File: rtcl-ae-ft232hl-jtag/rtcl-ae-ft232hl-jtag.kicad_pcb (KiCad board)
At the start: 2 copper layers, 20.3 x 52.1 mm, 3 parts, among them J1 Conn_01x14, J2 Conn_01x14, J3 Conn_01x06

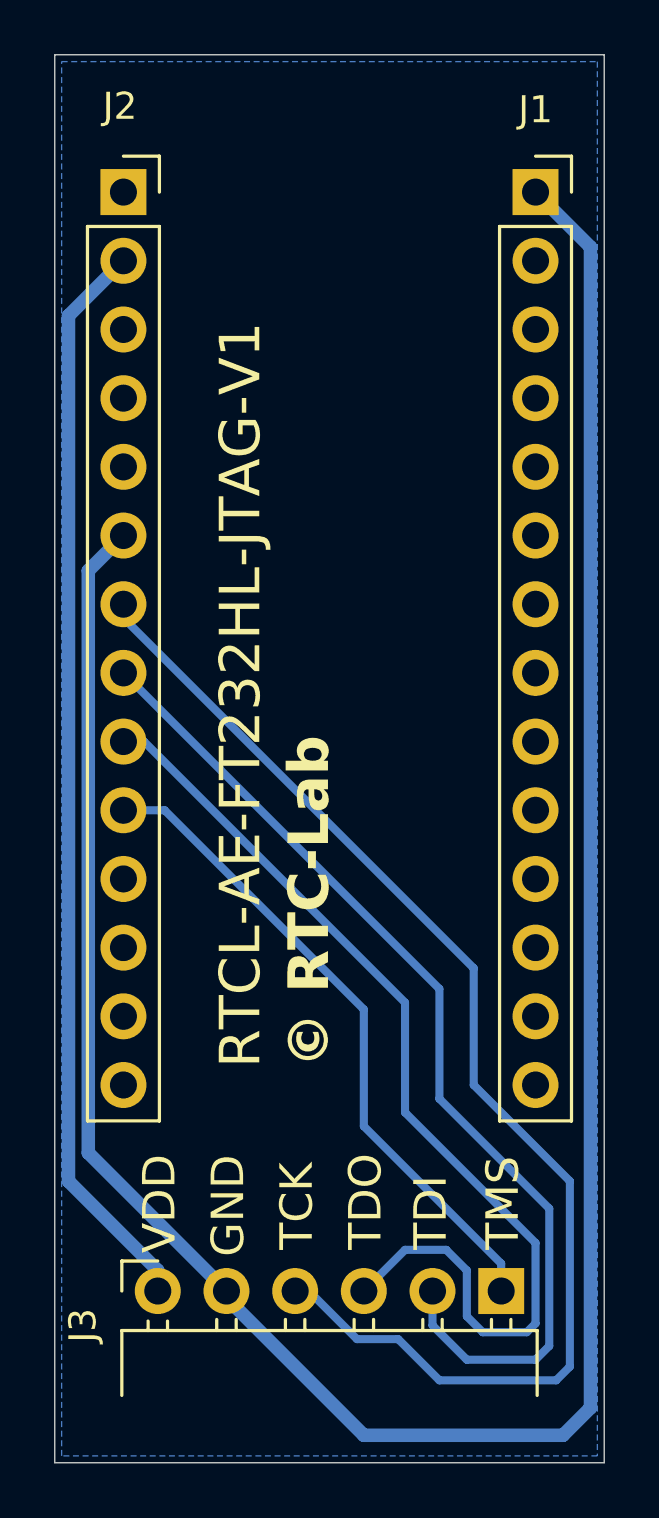
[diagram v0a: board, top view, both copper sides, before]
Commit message: Update KiCad project settings for improved layer visibility and clearance
- Changed active layer from 2 to 7 in the .kicad_prl file to enhance design focus.
- Updated layer visibility settings: enabled text display and disabled track display.
- Adjusted zone display mode from 0 to 1 for better zone management.
- Modified solder mask to copper clearance from 0.0 to 0.005 in the .kicad_pro file for improved manufacturing tolerances.
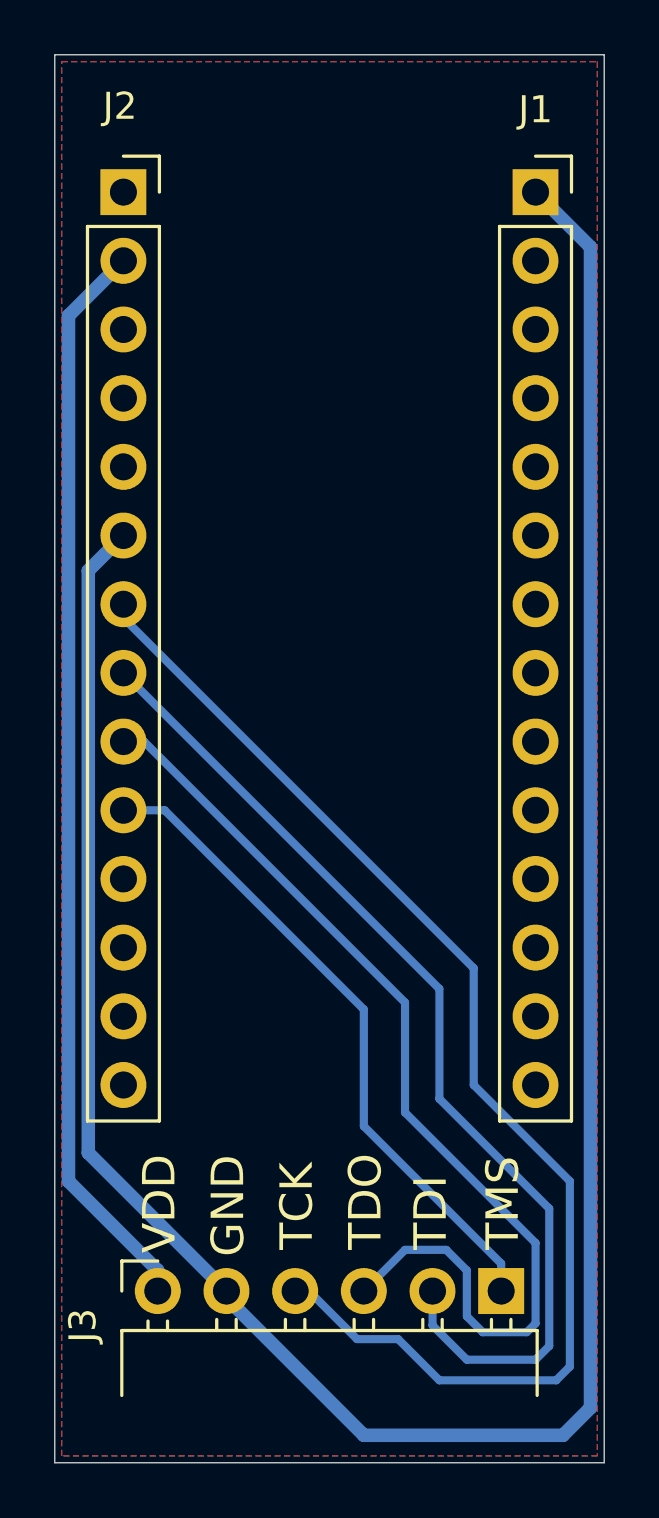
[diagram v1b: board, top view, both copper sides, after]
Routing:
- added copper zone on F.Cu, net GND
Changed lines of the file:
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@@
+		)
+	)
+	(gr_text "VDD"
+		(at 119.888 125.476 -90)
+		(layer "B.SilkS")
+		(effects
+			(font
+				(size 1.2 1.2)
+				(thickness 0.15)
+			)
+			(justify left bottom mirror)
+		)
+	)
+	(gr_text "GND"
+		(at 122.428 125.73 -90)
+		(layer "B.SilkS")
+		(effects
+			(font
+				(size 1.2 1.2)
+				(thickness 0.15)
+			)
+			(justify left bottom mirror)
+		)
+	)
+	(gr_text "TCK"
+		(at 124.968 125.476 -90)
+		(layer "B.SilkS")
+		(effects
+			(font
+				(size 1.2 1.2)
+				(thickness 0.15)
+			)
+			(justify left bottom mirror)
+		)
+	)
+	(gr_text "TDO"
+		(at 127.508 125.476 -90)
+		(layer "B.SilkS")
+		(effects
+			(font
+				(size 1.2 1.2)
+				(thickness 0.15)
+			)
+			(justify left bottom mirror)
+		)
+	)
+	(gr_text "TDI"
+		(at 130.048 125.476 -90)
+		(layer "B.SilkS")
+		(effects
+			(font
+				(size 1.2 1.2)
+				(thickness 0.15)
+			)
+			(justify left bottom mirror)
+		)
+	)
+	(gr_text "TMS"
+		(at 132.588 125.476 -90)
+		(layer "B.SilkS")
+		(effects
+			(font
+				(size 1.2 1.2)
+				(thickness 0.15)
+			)
+			(justify left bottom mirror)
 		)
 	)
 	(gr_text "RTCL-AE-FT232HL-JTAG-V1"
-		(at 124.587 118.745 90)
-		(layer "F.SilkS")
+		(at 130.302 118.618 -90)
+		(layer "B.SilkS")
 		(effects
 			(font
@@
 				(thickness 0.2)
 			)
-			(justify left bottom)
+			(justify left bottom mirror)
 		)
 	)
 	(gr_text "© RTC-Lab"
-		(at 127.127 118.745 90)
-		(layer "F.SilkS")
+		(at 127.508 118.745 -90)
+		(layer "B.SilkS")
 		(effects
 			(font
@@
 				(bold yes)
 			)
-			(justify left bottom)
+			(justify left bottom mirror)
 		)
 	)
@@
 	(zone
 		(net "GND")
-		(layer "B.Cu")
+		(layers "F.Cu" "B.Cu")
 		(name "GND")
 		(hatch edge 0.5)
